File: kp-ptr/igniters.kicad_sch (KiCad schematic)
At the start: 36 parts, among them J10 Conn_01x02, J11 Conn_01x02, J12 Conn_01x02, J13 Conn_01x02, Q2 DMC2025UFDB_v2, Q3 DMC2025UFDB_v2, Q4 DMC2025UFDB_v2, Q5 DMC2025UFDB_v2

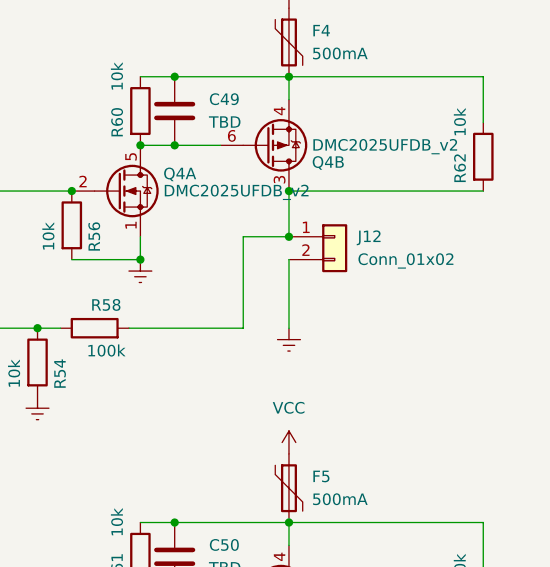
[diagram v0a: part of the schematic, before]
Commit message: chyba wszystkie footprinty
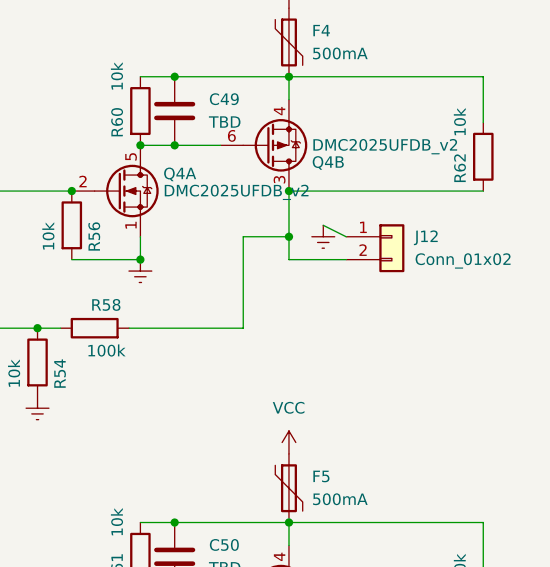
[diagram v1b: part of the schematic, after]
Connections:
- net Earth: now also J12.1 (Pin_1); no longer J12.2 (Pin_2)
- net at Q4.3 (D2), R58.2, R62.2: now also J12.2 (Pin_2); no longer J12.1 (Pin_1)
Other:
- moved on the sheet: J12

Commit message: PCB update
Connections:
- net Earth: now also J10.1 (Pin_1), J11.1 (Pin_1), J13.1 (Pin_1); no longer J10.2 (Pin_2), J11.2 (Pin_2), J13.2 (Pin_2)
- net at Q3.3 (D2), R49.2, R53.2: now also J11.2 (Pin_2); no longer J11.1 (Pin_1)
- net at Q5.3 (D2), R59.2, R63.2: now also J13.2 (Pin_2); no longer J13.1 (Pin_1)
- net at Q2.3 (D2), R48.2, R52.2: now also J10.2 (Pin_2); no longer J10.1 (Pin_1)
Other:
- moved on the sheet: J12
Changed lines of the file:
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@@
-    (stroke (width 0) (type default) (color 0 0 0 0))
-  )
-  (wire (pts (xy 173.99 83.82) (xy 176.53 85.09))
     (stroke (width 0) (type default) (color 0 0 0 0))
   )
@@
     (pin "6")
   )
-  (symbol (lib_id "Connector_Generic:Conn_01x02") (at 175.26 134.62 0) (unit 1)
-    (in_bom yes) (on_board yes) (fields_autoplaced)
-    (property "Reference" "J13" (id 0) (at 177.8 134.6199 0)
-      (effects (font (size 1.27 1.27)) (justify left))
-    )
-    (property "Value" "Conn_01x02" (id 1) (at 177.8 137.1599 0)
-      (effects (font (size 1.27 1.27)) (justify left))
-    )
-    (property "Footprint" "TerminalBlock_TE-Connectivity:TerminalBlock_TE_282834-2_1x02_P2.54mm_Horizontal" (id 2) (at 175.26 134.62 0)
-      (effects (font (size 1.27 1.27)) hide)
-    )
-    (property "Datasheet" "~" (id 3) (at 175.26 134.62 0)
+  (symbol (lib_id "Connector_Generic:Conn_01x02") (at 175.26 137.16 0) (mirror x) (unit 1)
+    (in_bom yes) (on_board yes) (fields_autoplaced)
+    (property "Reference" "J13" (id 0) (at 175.26 128.27 0))
+    (property "Value" "Conn_01x02" (id 1) (at 175.26 130.81 0))
+    (property "Footprint" "TerminalBlock_TE-Connectivity:TerminalBlock_TE_282834-2_1x02_P2.54mm_Horizontal" (id 2) (at 175.26 137.16 0)
+      (effects (font (size 1.27 1.27)) hide)
+    )
+    (property "Datasheet" "~" (id 3) (at 175.26 137.16 0)
       (effects (font (size 1.27 1.27)) hide)
     )
@@
     (pin "2")
   )
-  (symbol (lib_id "Connector_Generic:Conn_01x02") (at 92.71 85.09 0) (unit 1)
-    (in_bom yes) (on_board yes) (fields_autoplaced)
-    (property "Reference" "J10" (id 0) (at 95.25 85.0899 0)
-      (effects (font (size 1.27 1.27)) (justify left))
-    )
-    (property "Value" "Conn_01x02" (id 1) (at 95.25 87.6299 0)
-      (effects (font (size 1.27 1.27)) (justify left))
-    )
-    (property "Footprint" "TerminalBlock_TE-Connectivity:TerminalBlock_TE_282834-2_1x02_P2.54mm_Horizontal" (id 2) (at 92.71 85.09 0)
-      (effects (font (size 1.27 1.27)) hide)
-    )
-    (property "Datasheet" "~" (id 3) (at 92.71 85.09 0)
+  (symbol (lib_id "Connector_Generic:Conn_01x02") (at 92.71 87.63 0) (mirror x) (unit 1)
+    (in_bom yes) (on_board yes) (fields_autoplaced)
+    (property "Reference" "J10" (id 0) (at 92.71 78.74 0))
+    (property "Value" "Conn_01x02" (id 1) (at 92.71 81.28 0))
+    (property "Footprint" "TerminalBlock_TE-Connectivity:TerminalBlock_TE_282834-2_1x02_P2.54mm_Horizontal" (id 2) (at 92.71 87.63 0)
+      (effects (font (size 1.27 1.27)) hide)
+    )
+    (property "Datasheet" "~" (id 3) (at 92.71 87.63 0)
       (effects (font (size 1.27 1.27)) hide)
     )
@@
     (pin "1")
   )
-  (symbol (lib_id "Connector_Generic:Conn_01x02") (at 181.61 85.09 0) (unit 1)
-    (in_bom yes) (on_board yes) (fields_autoplaced)
-    (property "Reference" "J12" (id 0) (at 184.15 85.0899 0)
-      (effects (font (size 1.27 1.27)) (justify left))
-    )
-    (property "Value" "Conn_01x02" (id 1) (at 184.15 87.6299 0)
-      (effects (font (size 1.27 1.27)) (justify left))
-    )
-    (property "Footprint" "TerminalBlock_TE-Connectivity:TerminalBlock_TE_282834-2_1x02_P2.54mm_Horizontal" (id 2) (at 181.61 85.09 0)
-      (effects (font (size 1.27 1.27)) hide)
-    )
-    (property "Datasheet" "~" (id 3) (at 181.61 85.09 0)
+  (symbol (lib_id "Connector_Generic:Conn_01x02") (at 181.61 90.17 0) (mirror x) (unit 1)
+    (in_bom yes) (on_board yes) (fields_autoplaced)
+    (property "Reference" "J12" (id 0) (at 181.61 81.28 0))
+    (property "Value" "Conn_01x02" (id 1) (at 181.61 83.82 0))
+    (property "Footprint" "TerminalBlock_TE-Connectivity:TerminalBlock_TE_282834-2_1x02_P2.54mm_Horizontal" (id 2) (at 181.61 90.17 0)
+      (effects (font (size 1.27 1.27)) hide)
+    )
+    (property "Datasheet" "~" (id 3) (at 181.61 90.17 0)
       (effects (font (size 1.27 1.27)) hide)
     )
@@
     (pin "1")
   )
-  (symbol (lib_id "Connector_Generic:Conn_01x02") (at 92.71 135.89 0) (unit 1)
-    (in_bom yes) (on_board yes) (fields_autoplaced)
-    (property "Reference" "J11" (id 0) (at 95.25 135.8899 0)
-      (effects (font (size 1.27 1.27)) (justify left))
-    )
-    (property "Value" "Conn_01x02" (id 1) (at 95.25 138.4299 0)
-      (effects (font (size 1.27 1.27)) (justify left))
-    )
-    (property "Footprint" "TerminalBlock_TE-Connectivity:TerminalBlock_TE_282834-2_1x02_P2.54mm_Horizontal" (id 2) (at 92.71 135.89 0)
-      (effects (font (size 1.27 1.27)) hide)
-    )
-    (property "Datasheet" "~" (id 3) (at 92.71 135.89 0)
+  (symbol (lib_id "Connector_Generic:Conn_01x02") (at 92.71 138.43 0) (mirror x) (unit 1)
+    (in_bom yes) (on_board yes) (fields_autoplaced)
+    (property "Reference" "J11" (id 0) (at 92.71 128.905 0))
+    (property "Value" "Conn_01x02" (id 1) (at 92.71 131.445 0))
+    (property "Footprint" "TerminalBlock_TE-Connectivity:TerminalBlock_TE_282834-2_1x02_P2.54mm_Horizontal" (id 2) (at 92.71 138.43 0)
+      (effects (font (size 1.27 1.27)) hide)
+    )
+    (property "Datasheet" "~" (id 3) (at 92.71 138.43 0)
       (effects (font (size 1.27 1.27)) hide)
     )
@@
     (pin "2")
   )
-  (symbol (lib_id "power:Earth") (at 173.99 83.82 0) (unit 1)
-    (in_bom yes) (on_board yes) (fields_autoplaced)
-    (property "Reference" "#PWR0173" (id 0) (at 173.99 90.17 0)
-      (effects (font (size 1.27 1.27)) hide)
-    )
-    (property "Value" "Earth" (id 1) (at 173.99 87.63 0)
-      (effects (font (size 1.27 1.27)) hide)
-    )
-    (property "Footprint" "" (id 2) (at 173.99 83.82 0)
-      (effects (font (size 1.27 1.27)) hide)
-    )
-    (property "Datasheet" "~" (id 3) (at 173.99 83.82 0)
-      (effects (font (size 1.27 1.27)) hide)
-    )
+  (symbol (lib_id "power:Earth") (at 176.53 90.17 0) (unit 1)
+    (in_bom yes) (on_board yes) (fields_autoplaced)
+    (property "Reference" "#PWR0173" (id 0) (at 176.53 96.52 0)
+      (effects (font (size 1.27 1.27)) hide)
+    )
+    (property "Value" "Earth" (id 1) (at 176.53 93.98 0)
+      (effects (font (size 1.27 1.27)) hide)
+    )
+    (property "Footprint" "" (id 2) (at 176.53 90.17 0)
+      (effects (font (size 1.27 1.27)) hide)
+    )
+    (property "Datasheet" "~" (id 3) (at 176.53 90.17 0)
+      (effects (font (size 1.27 1.27)) hide)
+    )

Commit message: SCH&PCB update
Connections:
- net IGN3_PWR: now reaches C48.1, F3.2, Q3.4 (S2), R51.1, R53.1
- net IGN4_PWR: now reaches C50.1, F5.2, Q5.4 (S2), R61.1, R63.1
- net IGN1_PWR: now reaches C47.1, F2.2, Q2.4 (S2), R50.1, R52.1
- net IGN2_PWR: now reaches C49.1, F4.2, Q4.4 (S2), R60.1, R62.1
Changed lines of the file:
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@@
     (stroke (width 0) (type default) (color 0 0 0 0))
+  )
+  (global_label "IGN4_PWR" (shape input) (at 191.77 116.84 90) (fields_autoplaced)
+    (effects (font (size 1.27 1.27)) (justify left))
+    (property "Intersheet References" "${INTERSHEET_REFS}" (id 0) (at 191.6906 105.0531 90)
+      (effects (font (size 1.27 1.27)) (justify left) hide)
+    )
   )
   (global_label "IGN3_DET" (shape input) (at 52.07 146.05 180) (fields_autoplaced)
@@
     (property "Intersheet References" "${INTERSHEET_REFS}" (id 0) (at 40.8879 145.9706 0)
       (effects (font (size 1.27 1.27)) (justify right) hide)
+    )
+  )
+  (global_label "IGN2_PWR" (shape input) (at 191.77 67.31 90) (fields_autoplaced)
+    (effects (font (size 1.27 1.27)) (justify left))
+    (property "Intersheet References" "${INTERSHEET_REFS}" (id 0) (at 191.6906 55.5231 90)
+      (effects (font (size 1.27 1.27)) (justify left) hide)
     )
   )
@@
     (property "Intersheet References" "${INTERSHEET_REFS}" (id 0) (at 123.4379 95.1706 0)
       (effects (font (size 1.27 1.27)) (justify right) hide)
+    )
+  )
+  (global_label "IGN3_PWR" (shape input) (at 109.22 118.11 90) (fields_autoplaced)
+    (effects (font (size 1.27 1.27)) (justify left))
+    (property "Intersheet References" "${INTERSHEET_REFS}" (id 0) (at 109.1406 106.3231 90)
+      (effects (font (size 1.27 1.27)) (justify left) hide)
     )
   )
@@
     )
   )
+  (global_label "IGN1_PWR" (shape input) (at 109.22 67.31 90) (fields_autoplaced)
+    (effects (font (size 1.27 1.27)) (justify left))
+    (property "Intersheet References" "${INTERSHEET_REFS}" (id 0) (at 109.1406 55.5231 90)
+      (effects (font (size 1.27 1.27)) (justify left) hide)
+    )
+  )

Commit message: Update from v0.1 to v1.0
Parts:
- C47, C48, C49, C50: value TBD -> 1uF
- F2, F3, F4, F5: footprint Fuse:Fuse_0805_2012Metric -> Fuse:Fuse_1210_3225Metric
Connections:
- net VCC: now also C47.1, C48.1, C49.1, C50.1, Q2.4 (S2), Q3.4 (S2), Q4.4 (S2), Q5.4 (S2), R50.1, R51.1, R52.1, R53.1, R60.1, R61.1, R62.1, R63.1; no longer F2.1, F3.1, F4.1, F5.1
- net at Q3.3 (D2), R49.2, R53.2: now also F3.1; no longer J11.2 (Pin_2)
- net at Q5.3 (D2), R59.2, R63.2: now also F5.1; no longer J13.2 (Pin_2)
- net at Q2.3 (D2), R48.2, R52.2: now also F2.1; no longer J10.2 (Pin_2)
- net at Q4.3 (D2), R58.2, R62.2: now also F4.1; no longer J12.2 (Pin_2)
- removed net IGN1_PWR: C47.1, F2.2, Q2.4 (S2), R50.1, R52.1
- removed net IGN2_PWR: C49.1, F4.2, Q4.4 (S2), R60.1, R62.1
- removed net IGN3_PWR: C48.1, F3.2, Q3.4 (S2), R51.1, R53.1
- removed net IGN4_PWR: C50.1, F5.2, Q5.4 (S2), R61.1, R63.1
- new net: F5.2, J13.2 (Pin_2)
- new net: F2.2, J10.2 (Pin_2)
- new net: F4.2, J12.2 (Pin_2)
- new net: F3.2, J11.2 (Pin_2)
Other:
- moved on the sheet: F2, F3, F4, F5, J10, J11, J12, J13

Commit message: Work in progress
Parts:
- F2, F3, F4, F5: footprint Fuse:Fuse_1210_3225Metric -> Fuse:Fuse_1206_3216Metric
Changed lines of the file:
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@@
       (effects (font (size 1.27 1.27)) (justify left))
     )
-    (property "Footprint" "Fuse:Fuse_1210_3225Metric" (id 2) (at 171.45 93.98 0)
+    (property "Footprint" "Fuse:Fuse_1206_3216Metric" (id 2) (at 171.45 93.98 0)
       (effects (font (size 1.27 1.27)) (justify left) hide)
     )
@@
       (effects (font (size 1.27 1.27)) (justify left))
     )
-    (property "Footprint" "Fuse:Fuse_1210_3225Metric" (id 2) (at 88.9 93.98 0)
+    (property "Footprint" "Fuse:Fuse_1206_3216Metric" (id 2) (at 88.9 93.98 0)
       (effects (font (size 1.27 1.27)) (justify left) hide)
     )
@@
       (effects (font (size 1.27 1.27)) (justify left))
     )
-    (property "Footprint" "Fuse:Fuse_1210_3225Metric" (id 2) (at 88.9 144.78 0)
+    (property "Footprint" "Fuse:Fuse_1206_3216Metric" (id 2) (at 88.9 144.78 0)
       (effects (font (size 1.27 1.27)) (justify left) hide)
     )
@@
       (effects (font (size 1.27 1.27)) (justify left))
     )
-    (property "Footprint" "Fuse:Fuse_1210_3225Metric" (id 2) (at 171.45 143.51 0)
-      (effects (font (size 1.27 1.27)) (justify left) hide)
-    )
+    (property "Footprint" "Fuse:Fuse_1206_3216Metric" (id 2) (at 171.45 143.51 0)
+      (effects (font (size 1.27 1.27)) (justify left) hide)
+    )

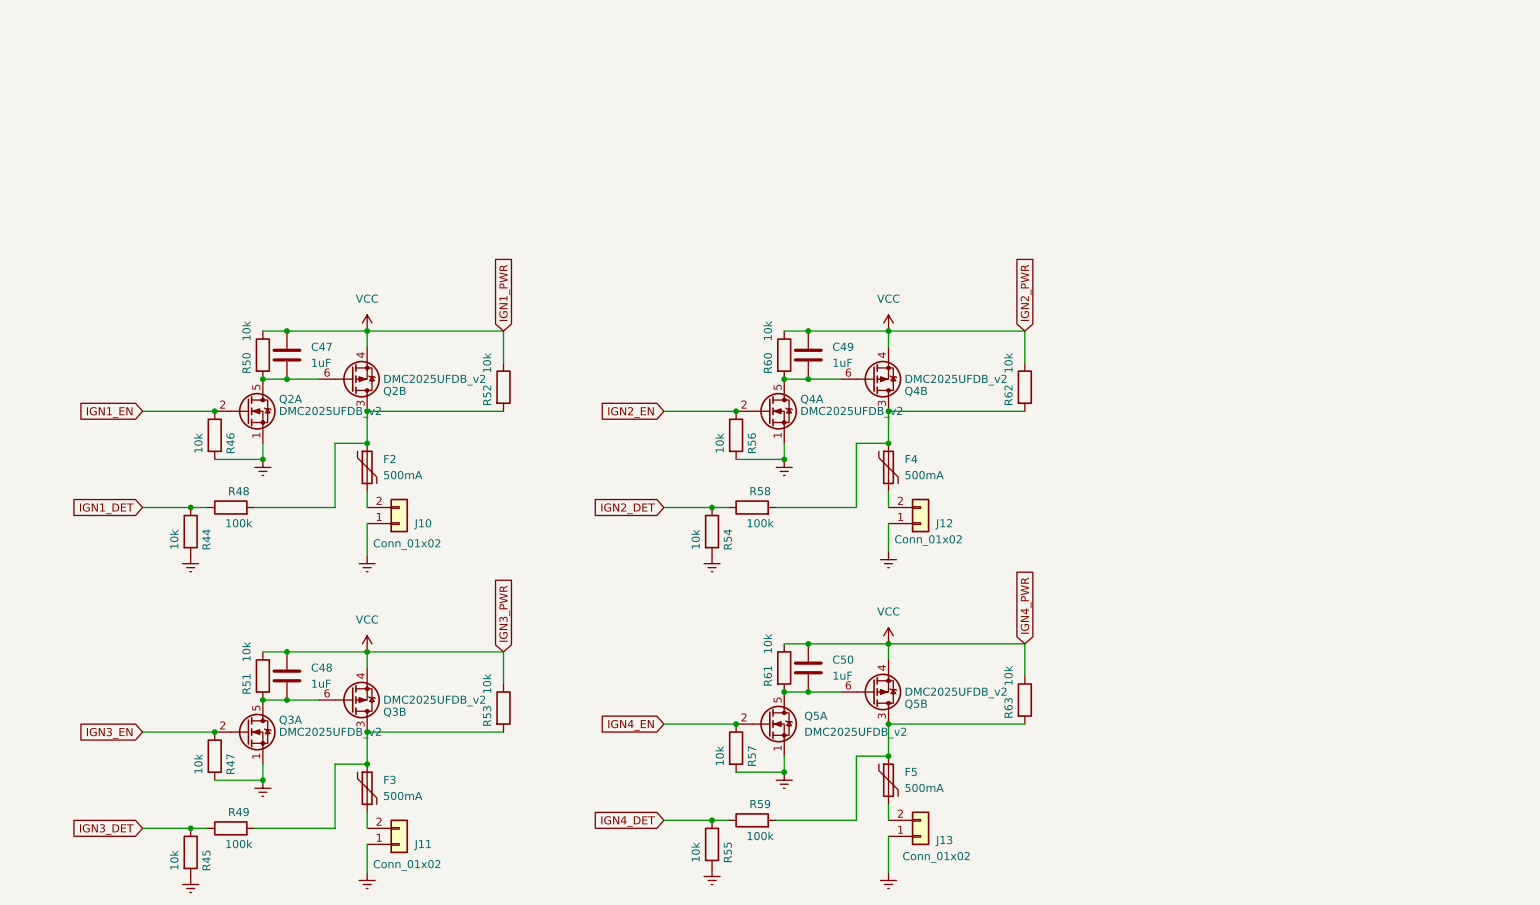
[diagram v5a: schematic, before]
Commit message: IGN detector update
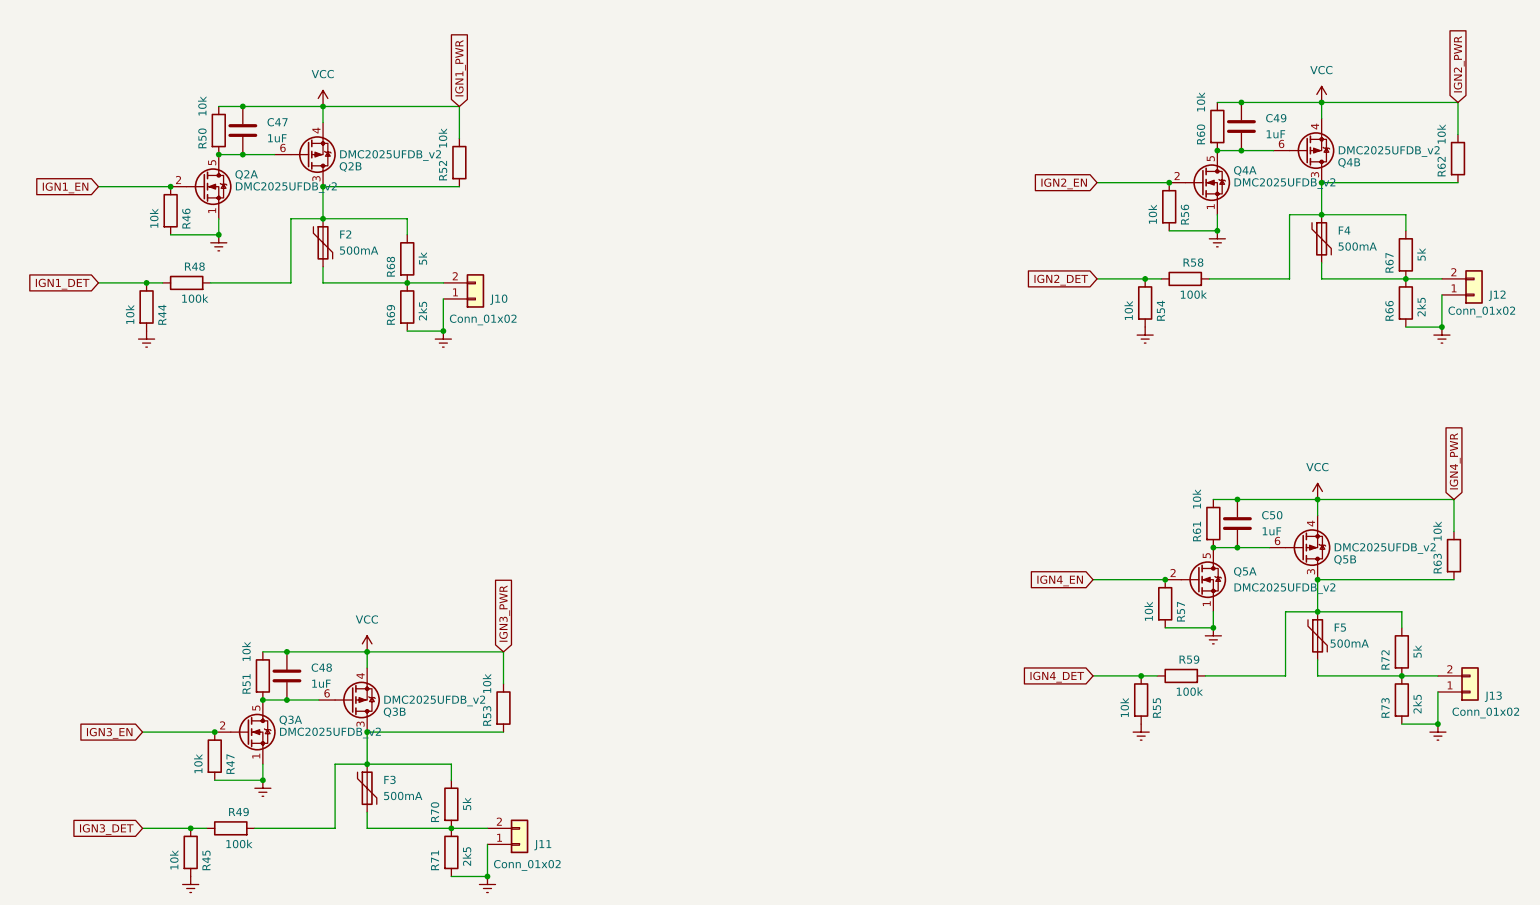
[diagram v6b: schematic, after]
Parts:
- added R66, R69, R71, R73: 2k5, Resistor_SMD:R_0402_1005Metric, symbol Device:R
- added R67, R68, R70, R72: 5k, Resistor_SMD:R_0402_1005Metric, symbol Device:R
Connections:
- net Earth: now also R66.2, R69.2, R71.2, R73.2
- net at F3.1, Q3.3 (D2), R49.2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: now also R70.1
- net at F5.1, Q5.3 (D2), R59.2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: now also R72.1
- net at F5.2, J13.2 (Pin_2): now also R72.2, R73.1
- net at F2.1, Q2.3 (D2), R48.2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: now also R68.1
- net at F2.2, J10.2 (Pin_2): now also R68.2, R69.1
- net at F4.1, Q4.3 (D2), R58.2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: now also R67.1
- net at F4.2, J12.2 (Pin_2): now also R66.1, R67.2
- net at F3.2, J11.2 (Pin_2): now also R70.2, R71.1
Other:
- moved on the sheet: C47, C49, C50, F2, F4, F5, J10, J11, J12, J13, Q2A, Q2B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
